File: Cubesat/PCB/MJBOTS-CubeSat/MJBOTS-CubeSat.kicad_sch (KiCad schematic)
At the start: 21 parts, among them J1 Display, J10 MOTOR3-XT30, J12 MOTOR3, J2 MPU 6050, J3 Pi_GPIO, J4 CAN, J5 MOTOR1, J6 MOTOR2, J7 INPUT-XT60, J8 MOTOR1-XT30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

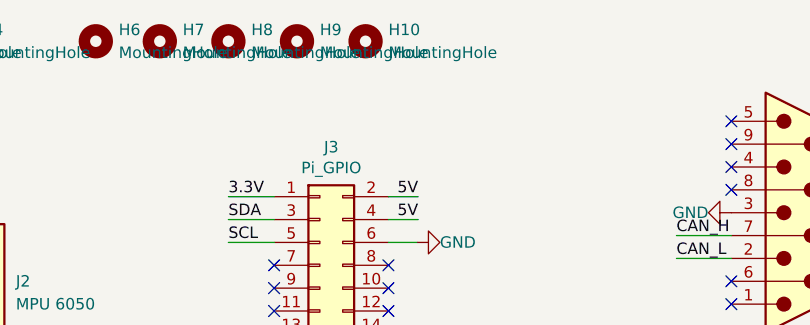
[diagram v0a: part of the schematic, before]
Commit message: Updated CubeSat PCB
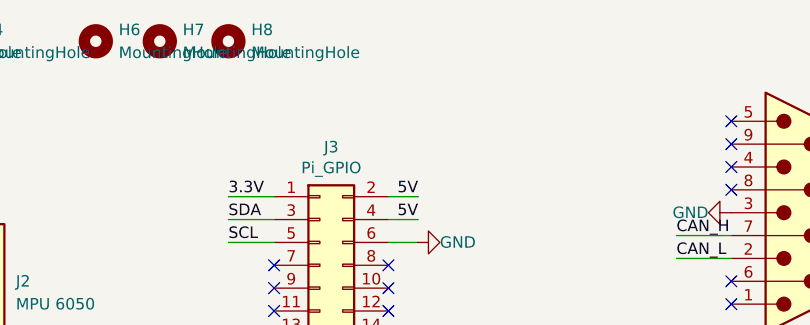
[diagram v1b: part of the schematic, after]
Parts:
- removed H10, H9: MountingHole, MountingHole:MountingHole_2.5mm, symbol Mechanical:MountingHole
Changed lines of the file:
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@@
     (effects (font (size 1.27 1.27)) (justify left bottom))
-  )
-  (symbol (lib_id "Mechanical:MountingHole") (at 167.132 40.64 0) (unit 1)
-    (in_bom yes) (on_board yes) (fields_autoplaced)
-    (property "Reference" "H10" (id 0) (at 169.672 39.3699 0)
-      (effects (font (size 1.27 1.27)) (justify left))
-    )
-    (property "Value" "MountingHole" (id 1) (at 169.672 41.9099 0)
-      (effects (font (size 1.27 1.27)) (justify left))
-    )
-    (property "Footprint" "MountingHole:MountingHole_2.5mm" (id 2) (at 167.132 40.64 0)
-      (effects (font (size 1.27 1.27)) hide)
-    )
-    (property "Datasheet" "~" (id 3) (at 167.132 40.64 0)
-      (effects (font (size 1.27 1.27)) hide)
-    )
   )
   (symbol (lib_id "Mechanical:MountingHole") (at 137.16 40.64 0) (unit 1)
@@
     (pin "3")
   )
-  (symbol (lib_id "Mechanical:MountingHole") (at 159.512 40.64 0) (unit 1)
-    (in_bom yes) (on_board yes) (fields_autoplaced)
-    (property "Reference" "H9" (id 0) (at 162.052 39.3699 0)
-      (effects (font (size 1.27 1.27)) (justify left))
-    )
-    (property "Value" "MountingHole" (id 1) (at 162.052 41.9099 0)
-      (effects (font (size 1.27 1.27)) (justify left))
-    )
-    (property "Footprint" "MountingHole:MountingHole_2.5mm" (id 2) (at 159.512 40.64 0)
-      (effects (font (size 1.27 1.27)) hide)
-    )
-    (property "Datasheet" "~" (id 3) (at 159.512 40.64 0)
-      (effects (font (size 1.27 1.27)) hide)
-    )
-  )
   (symbol (lib_id "power:GND") (at 120.65 67.31 270) (unit 1)
     (in_bom yes) (on_board yes)
@@
       (reference "H8") (unit 1) (value "MountingHole") (footprint "MountingHole:MountingHole_2.5mm")
     )
-    (path "/f5fa2ee5-3f02-485d-b088-f57bfcd5766c"
-      (reference "H9") (unit 1) (value "MountingHole") (footprint "MountingHole:MountingHole_2.5mm")
-    )
-    (path "/07ffda05-0442-4468-90a5-d8332a022025"
-      (reference "H10") (unit 1) (value "MountingHole") (footprint "MountingHole:MountingHole_2.5mm")
-    )
     (path "/d5de051d-d0f2-40e1-9291-05aae056795f"

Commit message: Final Updates "HOPEFULLY"
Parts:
- removed H8: MountingHole, MountingHole:MountingHole_2.5mm, symbol Mechanical:MountingHole
- added H5: MountingHole, MountingHole:MountingHole_2.5mm, symbol Mechanical:MountingHole
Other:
- sheet A-D Converter ports: added VCC; removed none
- moved on the sheet: H6
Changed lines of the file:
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@@
 (kicad_sch (version 20211123) (generator eeschema)
   (paper "A4")
+  (junction (at 76.962 96.266) (diameter 0) (color 0 0 0 0)
+  )
   (no_connect (at 156.972 98.552))
   (no_connect (at 156.972 65.532))
@@
     (stroke (width 0) (type default) (color 0 0 0 0))
   )
+  (wire (pts (xy 55.372 133.35) (xy 59.944 133.35))
+    (stroke (width 0) (type default) (color 0 0 0 0))
+  )
   (wire (pts (xy 151.892 60.452) (xy 156.972 60.452))
     (stroke (width 0) (type default) (color 0 0 0 0))
@@
     (effects (font (size 1.27 1.27)) (justify left bottom))
   )
+  (label "VCC" (at 55.372 133.35 0)
+    (effects (font (size 1.27 1.27)) (justify left bottom))
+  )
   (label "5V" (at 135.382 90.424 180)
     (effects (font (size 1.27 1.27)) (justify right bottom))
@@
     (effects (font (size 1.27 1.27)) (justify left bottom))
   )
-  (symbol (lib_id "Mechanical:MountingHole") (at 137.16 40.64 0) (unit 1)
-    (in_bom yes) (on_board yes) (fields_autoplaced)
-    (property "Reference" "H6" (id 0) (at 139.7 39.3699 0)
-      (effects (font (size 1.27 1.27)) (justify left))
-    )
-    (property "Value" "MountingHole" (id 1) (at 139.7 41.9099 0)
-      (effects (font (size 1.27 1.27)) (justify left))
-    )
-    (property "Footprint" "MountingHole:MountingHole_2.5mm" (id 2) (at 137.16 40.64 0)
-      (effects (font (size 1.27 1.27)) hide)
-    )
-    (property "Datasheet" "~" (id 3) (at 137.16 40.64 0)
+  (symbol (lib_id "Mechanical:MountingHole") (at 130.048 40.64 0) (unit 1)
+    (in_bom yes) (on_board yes) (fields_autoplaced)
+    (property "Reference" "H6" (id 0) (at 132.588 39.3699 0)
+      (effects (font (size 1.27 1.27)) (justify left))
+    )
+    (property "Value" "MountingHole" (id 1) (at 132.588 41.9099 0)
+      (effects (font (size 1.27 1.27)) (justify left))
+    )
+    (property "Footprint" "MountingHole:MountingHole_2.5mm" (id 2) (at 130.048 40.64 0)
+      (effects (font (size 1.27 1.27)) hide)
+    )
+    (property "Datasheet" "~" (id 3) (at 130.048 40.64 0)
       (effects (font (size 1.27 1.27)) hide)
     )
@@
     (pin "2")
   )
+  (symbol (lib_id "power:PWR_FLAG") (at 76.962 96.266 0) (unit 1)
+    (in_bom yes) (on_board yes) (fields_autoplaced)
+    (property "Reference" "#FLG0102" (id 0) (at 76.962 94.361 0)
+      (effects (font (size 1.27 1.27)) hide)
+    )
+    (property "Value" "PWR_FLAG" (id 1) (at 76.962 91.44 0))
+    (property "Footprint" "" (id 2) (at 76.962 96.266 0)
+      (effects (font (size 1.27 1.27)) hide)
+    )
+    (property "Datasheet" "~" (id 3) (at 76.962 96.266 0)
+      (effects (font (size 1.27 1.27)) hide)
+    )
+    (pin "1")
+  )
   (symbol (lib_id "power:GND") (at 76.454 77.978 0) (unit 1)
     (in_bom yes) (on_board yes)
@@
       (effects (font (size 1.27 1.27)) hide)
     )
-    (property "Value" "GND" (id 1) (at 62.992 80.518 90)
+    (property "Value" "GND" (id 1) (at 64.008 80.518 90)
       (effects (font (size 1.27 1.27)) (justify right))
     )
@@
     )
   )
+  (symbol (lib_id "Mechanical:MountingHole") (at 145.542 40.64 0) (unit 1)
+    (in_bom yes) (on_board yes) (fields_autoplaced)
+    (property "Reference" "H7" (id 0) (at 148.082 39.3699 0)
+      (effects (font (size 1.27 1.27)) (justify left))
+    )
+    (property "Value" "MountingHole" (id 1) (at 148.082 41.9099 0)
+      (effects (font (size 1.27 1.27)) (justify left))
+    )
+    (property "Footprint" "MountingHole:MountingHole_2.5mm" (id 2) (at 145.542 40.64 0)
+      (effects (font (size 1.27 1.27)) hide)
+    )
+    (property "Datasheet" "~" (id 3) (at 145.542 40.64 0)
+      (effects (font (size 1.27 1.27)) hide)
+    )
+  )
   (symbol (lib_id "24V_Li_batt:Conn_01x03") (at 214.63 91.186 0) (unit 1)
     (in_bom yes) (on_board yes) (fields_autoplaced)
@@
     (pin "1")
   )
-  (symbol (lib_id "Mechanical:MountingHole") (at 144.272 40.64 0) (unit 1)
-    (in_bom yes) (on_board yes) (fields_autoplaced)
-    (property "Reference" "H7" (id 0) (at 146.812 39.3699 0)
-      (effects (font (size 1.27 1.27)) (justify left))
-    )
-    (property "Value" "MountingHole" (id 1) (at 146.812 41.9099 0)
-      (effects (font (size 1.27 1.27)) (justify left))
-    )
-    (property "Footprint" "MountingHole:MountingHole_2.5mm" (id 2) (at 144.272 40.64 0)
-      (effects (font (size 1.27 1.27)) hide)
-    )
-    (property "Datasheet" "~" (id 3) (at 144.272 40.64 0)
+  (symbol (lib_id "Mechanical:MountingHole") (at 137.414 40.64 0) (unit 1)
+    (in_bom yes) (on_board yes) (fields_autoplaced)
+    (property "Reference" "H5" (id 0) (at 139.954 39.3699 0)
+      (effects (font (size 1.27 1.27)) (justify left))
+    )
+    (property "Value" "MountingHole" (id 1) (at 139.954 41.9099 0)
+      (effects (font (size 1.27 1.27)) (justify left))
+    )
+    (property "Footprint" "MountingHole:MountingHole_2.5mm" (id 2) (at 137.414 40.64 0)
+      (effects (font (size 1.27 1.27)) hide)
+    )
+    (property "Datasheet" "~" (id 3) (at 137.414 40.64 0)
       (effects (font (size 1.27 1.27)) hide)
     )
@@
     (pin "5")
     (pin "6")
-  )
-  (symbol (lib_id "Mechanical:MountingHole") (at 151.892 40.64 0) (unit 1)
-    (in_bom yes) (on_board yes) (fields_autoplaced)
-    (property "Reference" "H8" (id 0) (at 154.432 39.3699 0)
-      (effects (font (size 1.27 1.27)) (justify left))
-    )
-    (property "Value" "MountingHole" (id 1) (at 154.432 41.9099 0)
-      (effects (font (size 1.27 1.27)) (justify left))
-    )
-    (property "Footprint" "MountingHole:MountingHole_2.5mm" (id 2) (at 151.892 40.64 0)
-      (effects (font (size 1.27 1.27)) hide)
-    )
-    (property "Datasheet" "~" (id 3) (at 151.892 40.64 0)
-      (effects (font (size 1.27 1.27)) hide)
-    )
   )
   (symbol (lib_id "Connector_Generic:Conn_02x20_Odd_Even") (at 162.052 80.772 0) (unit 1)
@@
       (effects (font (size 1.27 1.27)) (justify left))
     )
+    (pin "VCC" input (at 59.944 133.35 180)
+      (effects (font (size 1.27 1.27)) (justify left))
+    )
   )
   (sheet_instances
@@
       (reference "#FLG0101") (unit 1) (value "PWR_FLAG") (footprint "")
     )
+    (path "/353dcdab-295b-4884-b99f-346e0d932e58"
+      (reference "#FLG0102") (unit 1) (value "PWR_FLAG") (footprint "")
+    )
     (path "/e720ff28-7203-4205-97be-458b252c135b"
       (reference "#PWR0101") (unit 1) (value "GND") (footprint "")
@@
       (reference "#PWR0115") (unit 1) (value "GND") (footprint "")
     )
+    (path "/f4ba3478-2c95-496a-9c27-457b9411cacb/508cb951-553a-42aa-98fb-8fbae1b6eb7d"
+      (reference "#PWR0116") (unit 1) (value "GND") (footprint "")
+    )
     (path "/c125495c-82f3-42db-8b42-bf22cefa9f79"
       (reference "H1") (unit 1) (value "MountingHole") (footprint "MountingHole:MountingHole_2.5mm")
@@
       (reference "H4") (unit 1) (value "MountingHole") (footprint "MountingHole:MountingHole_2.5mm")
     )
+    (path "/b6794ca9-37d2-4959-ad5a-b6899fdc0e43"
+      (reference "H5") (unit 1) (value "MountingHole") (footprint "MountingHole:MountingHole_2.5mm")
+    )
     (path "/20538c33-4b7b-4c78-9d68-b98cd9361aea"
       (reference "H6") (unit 1) (value "MountingHole") (footprint "MountingHole:MountingHole_2.5mm")
     )
-    (path "/ab523916-fa2e-4753-93b6-47b9afdd276b"
+    (path "/6ea51669-04b2-4d14-bdca-acba8fa3ebde"
       (reference "H7") (unit 1) (value "MountingHole") (footprint "MountingHole:MountingHole_2.5mm")
-    )
-    (path "/da6f9729-f218-46e4-b198-41468c381a9f"
-      (reference "H8") (unit 1) (value "MountingHole") (footprint "MountingHole:MountingHole_2.5mm")
     )
     (path "/d5de051d-d0f2-40e1-9291-05aae056795f"
@@
       (reference "J10") (unit 1) (value "MOTOR3-XT30") (footprint "cube:XT30PWM")
     )
-    (path "/f4ba3478-2c95-496a-9c27-457b9411cacb/beb10ef3-eb97-446c-b630-ee80bacfd364"
-      (reference "J11") (unit 1) (value "JST-BATT") (footprint "Connector_PinHeader_2.54mm:PinHeader_1x04_P2.54mm_Vertical")
-    )
     (path "/fe307aa7-3d5b-431f-be0c-bc0fbe8002f0"
       (reference "J12") (unit 1) (value "MOTOR3") (footprint "Connector_PinHeader_2.54mm:PinHeader_1x03_P2.54mm_Vertical")
     )
+    (path "/f4ba3478-2c95-496a-9c27-457b9411cacb/15aa997a-aa5a-45f8-8a4d-cd6b3343a02a"
+      (reference "R1") (unit 1) (value "2k") (footprint "Resistor_SMD:R_0805_2012Metric_Pad1.20x1.40mm_HandSolder")
+    )
+    (path "/f4ba3478-2c95-496a-9c27-457b9411cacb/ba176358-80f6-4f7a-9db6-3bd603290649"
+      (reference "R2") (unit 1) (value "1k") (footprint "Resistor_SMD:R_0805_2012Metric_Pad1.20x1.40mm_HandSolder")
+    )
     (path "/56f63a98-abd0-410c-bb66-f75481e1c26f"
